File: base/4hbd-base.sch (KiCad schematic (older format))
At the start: 13 parts, among them J1 Screw_Terminal_01x03, J10 Screw_Terminal_01x04, J11 Screw_Terminal_01x02, J12 Conn_01x03, J13 Conn_01x08, J2 Screw_Terminal_01x03, J3 Screw_Terminal_01x03, J4 Screw_Terminal_01x03, J5 Screw_Terminal_01x02, J6 Screw_Terminal_01x02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

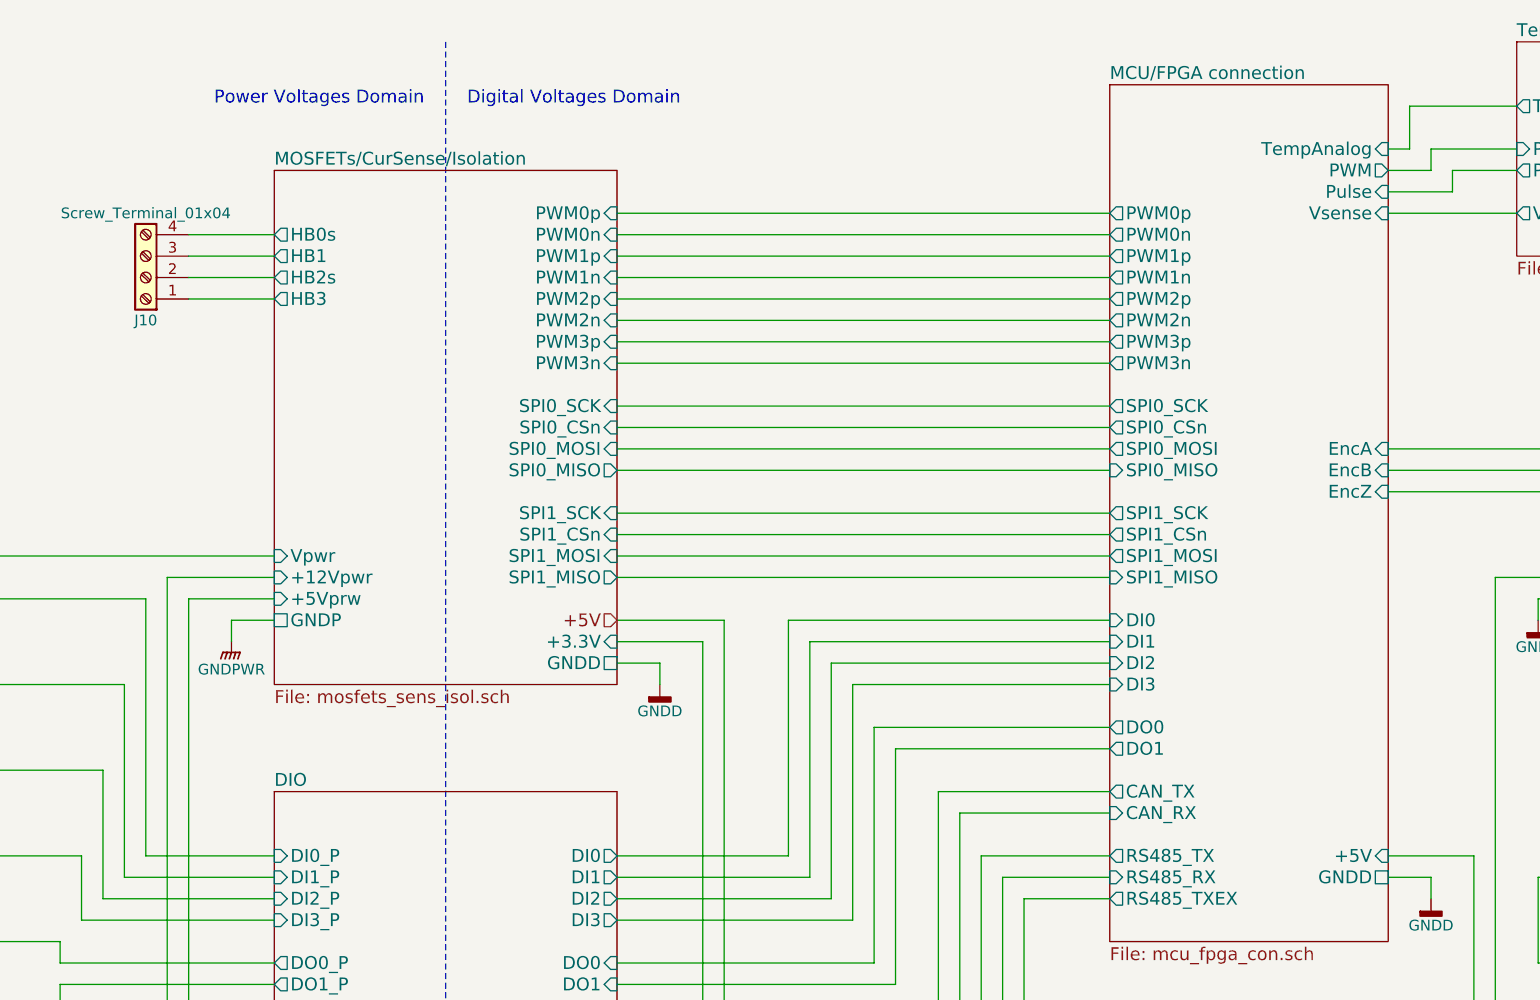
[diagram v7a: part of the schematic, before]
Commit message: Update schematics: 1. Connect analog voltages to MCU board connector 2. Implement Power DC/DC
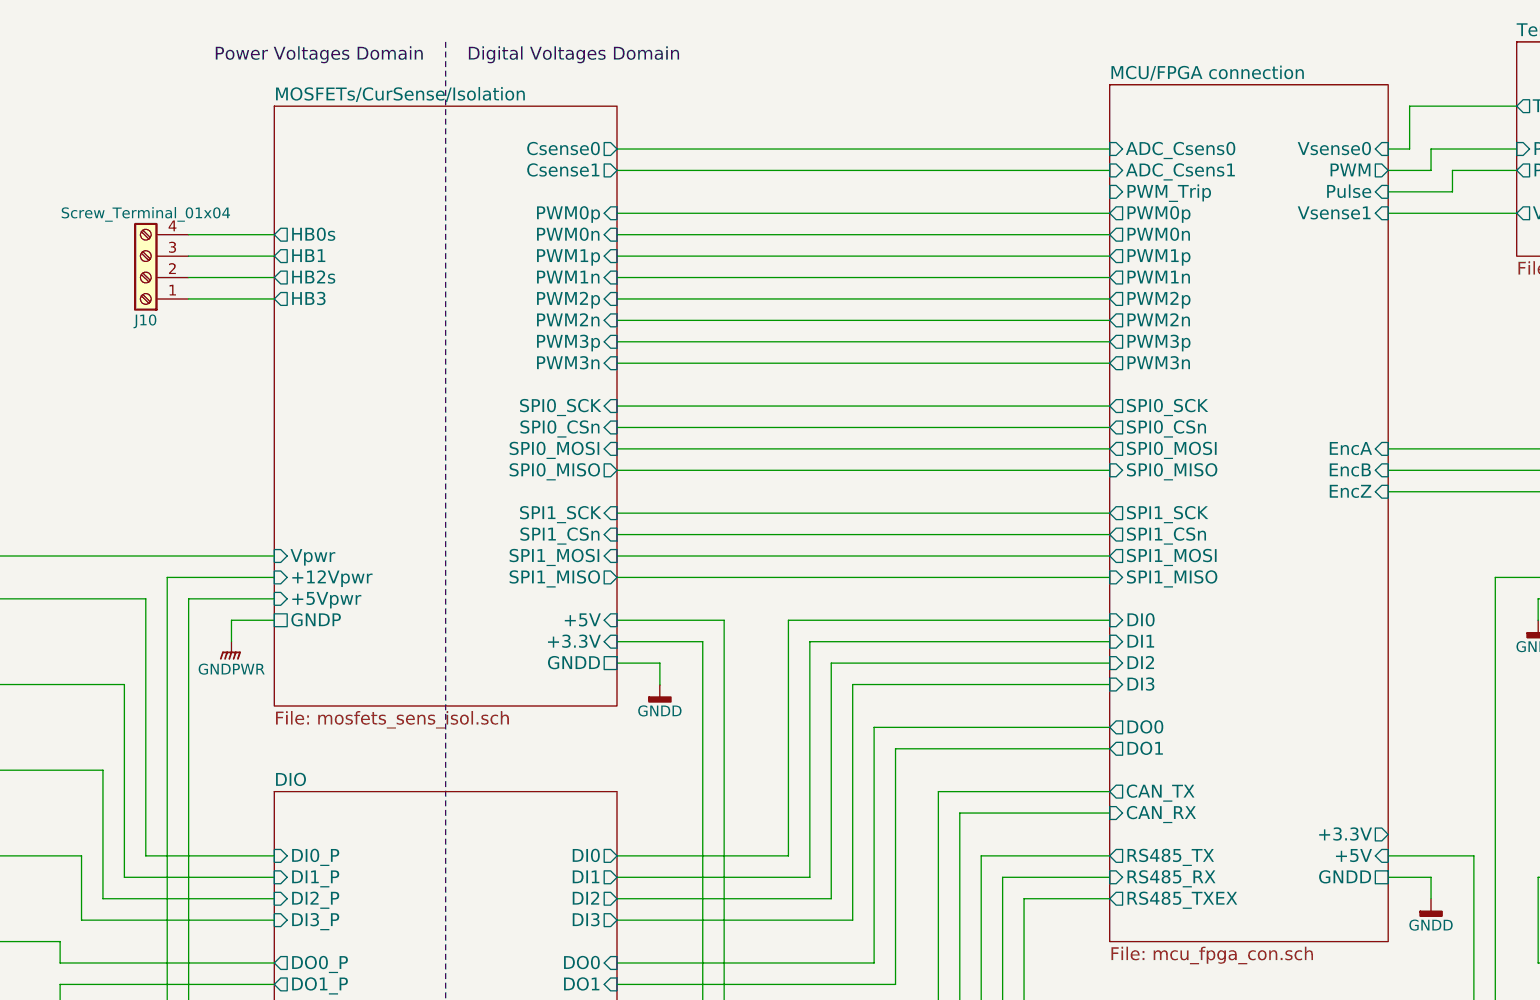
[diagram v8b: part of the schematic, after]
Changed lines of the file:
@@
 $EndDescr
 $Sheet
-S 3000 1400 1600 2400
+S 3000 1100 1600 2800
 U 5A1B9486
 F0 "MOSFETs/CurSense/Isolation" 60
@@
 F24 "Vpwr" I L 3000 3200 60
 F25 "+12Vpwr" I L 3000 3300 60
-F26 "+5Vprw" I L 3000 3400 60
-F27 "GNDP" U L 3000 3500 60
+F26 "GNDP" U L 3000 3500 60
+F27 "+5Vpwr" I L 3000 3400 60
+F28 "+5V" I R 4600 3500 60
+F29 "Csense0" O R 4600 1300 60
+F30 "Csense1" O R 4600 1400 60
 $EndSheet
 $Sheet
@@
 F16 "+12V" I L 3000 5400 60
 $EndSheet
-Text Notes 3700 1100 2    60   ~ 0
+Text Notes 3700 900  2    60   ~ 0
 Power Voltages Domain
-Text Notes 3900 1100 0    60   ~ 0
+Text Notes 3900 900  0    60   ~ 0
 Digital Voltages Domain
 $Sheet
@@
 F32 "EncB" I R 8200 2800 60
 F33 "EncZ" I R 8200 2900 60
-F34 "TempAnalog" I R 8200 1300 60
-F35 "PWM" O R 8200 1400 60
-F36 "Pulse" I R 8200 1500 60
-F37 "Vsense" I R 8200 1600 60
+F34 "PWM" O R 8200 1400 60
+F35 "Pulse" I R 8200 1500 60
+F36 "Vsense1" I R 8200 1600 60
+F37 "+3.3V" O R 8200 4500 60
+F38 "PWM_Trip" I L 6900 1500 60
+F39 "Vsense0" I R 8200 1300 60
+F40 "ADC_Csens1" I L 6900 1400 60
+F41 "ADC_Csens0" I L 6900 1300 60
 $EndSheet
 $Sheet
@@
 	5100 3500 4600 3500
 Connection ~ 8600 5300
-Text HLabel 4600 3500 0    60   Input ~ 0
-+5V
 Wire Wire Line
 	3000 5400 2500 5400
@@
 Wire Wire Line
 	10400 5200 10400 1400
+Wire Wire Line
+	4600 1300 6900 1300
+Wire Wire Line
+	4600 1400 6900 1400
 $EndSCHEMATC
